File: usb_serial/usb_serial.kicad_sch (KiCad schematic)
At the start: 13 parts, among them J1 47589-1001, J3 Conn_01x04_Pin, U1 FT232RL

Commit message: BOM generated
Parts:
- C1: Manufacturer (none) -> Kemet; Package (none) -> 0402; Part (none) -> C0402C103K5RECAUTO
- C2: Manufacturer (none) -> Samsung Electro-Mechanics; Package (none) -> 0805; Part (none) -> CL21A475KAQNNNE
- C3, C4: Manufacturer (none) -> Samsung Electro-Mechanics; Package (none) -> 0402; Part (none) -> CL05B104KP5NNNC
- D1, D2, D3: Manufacturer (none) -> LS R976-NR-1-0-20-R18; Package (none) -> 0805; Part (none) -> ams-OSRAM USA INC.
- J1: Manufacturer (none) -> Molex; Package None -> -; Part (none) -> 47589-1001
- J3: Manufacturer (none) -> Würth Elektronik; Package (none) -> -; Part (none) -> 61300411121
- R1, R2: Manufacturer (none) -> YAGEO; Package (none) -> 0402; Part (none) -> RC0402JR-0710KL
- R3: value 2.2k -> 1k; Manufacturer (none) -> YAGEO; Package (none) -> 0402; Part (none) -> RC0402JR-0710KL
- U1: Manufacturer (none) -> FTDI; Package (none) -> SSOP-28; Part (none) -> FT232RL

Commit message: BOM Fix  - wrong reg value
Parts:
- R1, R2, R3: Manufacturer YAGEO -> UNI-ROYAL(Uniroyal Elec); Part RC0402JR-0710KL -> 0402WGF1001TCE
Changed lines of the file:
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@@
 			)
 		)
-		(property "Manufacturer" "YAGEO"
+		(property "Manufacturer" "UNI-ROYAL(Uniroyal Elec)"
 			(at 226.06 102.87 0)
 			(effects
@@
 			)
 		)
-		(property "Part" "RC0402JR-0710KL"
+		(property "Part" "0402WGF1001TCE"
 			(at 226.06 102.87 0)
 			(effects
@@
 			)
 		)
-		(property "Manufacturer" "YAGEO"
+		(property "Manufacturer" "UNI-ROYAL(Uniroyal Elec)"
 			(at 102.87 86.36 0)
 			(effects
@@
 			)
 		)
-		(property "Part" "RC0402JR-0710KL"
+		(property "Part" "0402WGF1001TCE"
 			(at 102.87 86.36 0)
 			(effects
@@
 			)
 		)
-		(property "Manufacturer" "YAGEO"
+		(property "Manufacturer" "UNI-ROYAL(Uniroyal Elec)"
 			(at 254 102.87 0)
 			(effects
@@
 			)
 		)
-		(property "Part" "RC0402JR-0710KL"
+		(property "Part" "0402WGF1001TCE"
 			(at 254 102.87 0)
 			(effects

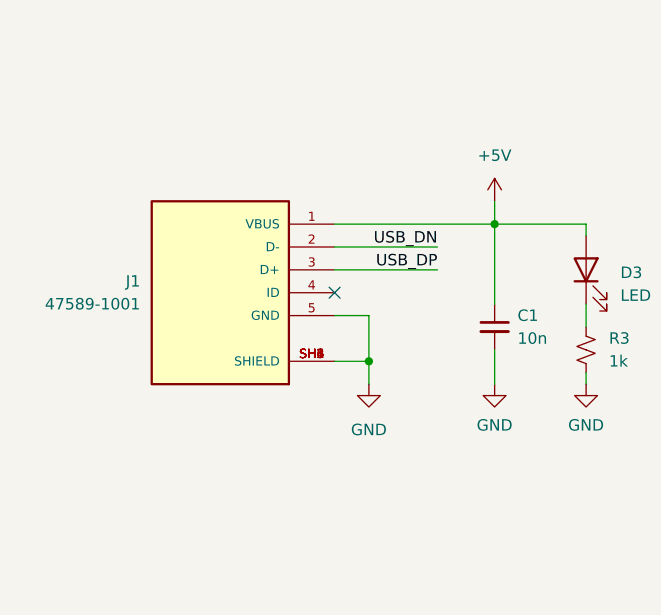
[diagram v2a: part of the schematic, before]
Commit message: JLCPCB adaptation - USB part changed
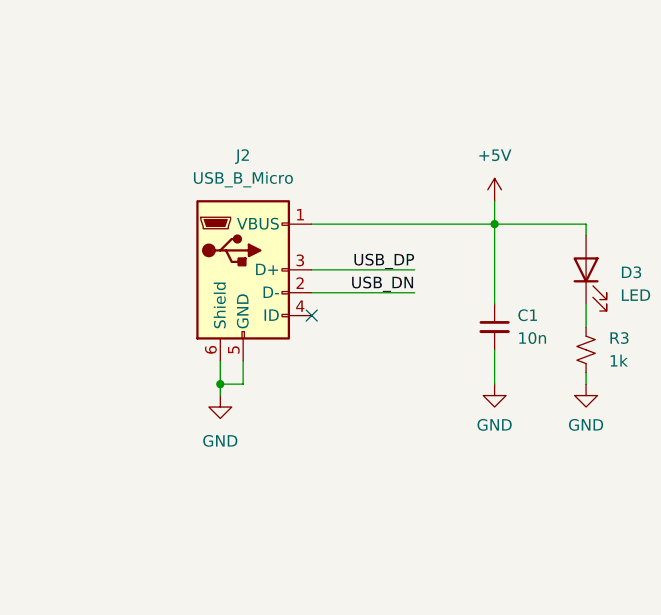
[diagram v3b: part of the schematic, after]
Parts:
- removed J1: 47589-1001, user_footprints:MOLEX_47589-1001, symbol 47589-1001:47589-1001
- added J2: USB_B_Micro, Connector_USB:USB_Micro-B_Amphenol_10118194-0001LF_Horizontal, symbol Connector:USB_B_Micro
- C1: footprint Capacitor_SMD:C_0402_1005Metric -> Capacitor_SMD:C_0603_1608Metric; Manufacturer Kemet -> FH (Guangdong Fenghua Advanced Tech); Package 0402 -> 0603; Part C0402C103K5RECAUTO -> 0603B103K500NT
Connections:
- net +5V: now also J2.1 (VBUS)
- net GND: now also J2.5 (GND), J2.6 (Shield)
- net USB_DN: now also J2.2 (D-)
- net USB_DP: now also J2.3 (D+)

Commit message: JLCPCB Ready - bom/Gerber/PnP/Schematic regenerated
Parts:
- C1: LCSC (none) -> C57112
- C2: LCSC (none) -> C1779
- C3, C4: LCSC (none) -> C133086
- D1, D2, D3: LCSC (none) -> C2899997
- J2: LCSC (none) -> C132563
- J3: LCSC (none) -> C5184785
- R1, R2, R3: LCSC (none) -> C11702
- U1: LCSC (none) -> C8690
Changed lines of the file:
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@@
 			)
 		)
+		(property "LCSC" "C133086"
+			(at 128.27 101.6 0)
+			(effects
+				(font
+					(size 1.27 1.27)
+				)
+				(hide yes)
+			)
+		)
 		(pin "1"
 		)
@@
 			)
 		)
+		(property "LCSC" "C8690"
+			(at 158.75 85.09 0)
+			(effects
+				(font
+					(size 1.27 1.27)
+				)
+				(hide yes)
+			)
+		)
 		(pin "8"
 		)
@@
 			)
 		)
+		(property "LCSC" "C2899997"
+			(at 102.87 77.47 0)
+			(effects
+				(font
+					(size 1.27 1.27)
+				)
+				(hide yes)
+			)
+		)
 		(pin "2"
 		)
@@
 			)
 		)
+		(property "LCSC" "C11702"
+			(at 226.06 102.87 0)
+			(effects
+				(font
+					(size 1.27 1.27)
+				)
+				(hide yes)
+			)
+		)
 		(pin "1"
 		)
@@
 			)
 		)
+		(property "LCSC" "C2899997"
+			(at 254 93.98 0)
+			(effects
+				(font
+					(size 1.27 1.27)
+				)
+				(hide yes)
+			)
+		)
 		(pin "2"
 		)
@@
 			)
 		)
+		(property "LCSC" "C1779"
+			(at 217.17 62.23 0)
+			(effects
+				(font
+					(size 1.27 1.27)
+				)
+				(hide yes)
+			)
+		)
 		(pin "1"
 		)
@@
 			)
 		)
+		(property "LCSC" "C132563"
+			(at 64.77 77.47 0)
+			(effects
+				(font
+					(size 1.27 1.27)
+				)
+				(hide yes)
+			)
+		)
 		(pin "1"
 		)
@@
 			)
 		)
+		(property "LCSC" "C133086"
+			(at 227.33 62.23 0)
+			(effects
+				(font
+					(size 1.27 1.27)
+				)
+				(hide yes)
+			)
+		)
 		(pin "1"
 		)
@@
 			)
 		)
+		(property "LCSC" "C11702"
+			(at 102.87 86.36 0)
+			(effects
+				(font
+					(size 1.27 1.27)
+				)
+				(hide yes)
+			)
+		)
 		(pin "1"
 		)
@@
 			)
 		)
+		(property "LCSC" "C5184785"
+			(at 228.6 134.62 0)
+			(effects
+				(font
+					(size 1.27 1.27)
+				)
+				(hide yes)
+			)
+		)
 		(pin "2"
 		)
@@
 			)
 		)
+		(property "LCSC" "C11702"
+			(at 254 102.87 0)
+			(effects
+				(font
+					(size 1.27 1.27)
+				)
+				(hide yes)
+			)
+		)
 		(pin "1"
 		)
@@
 			)
 		)
+		(property "LCSC" "C57112"
+			(at 92.71 83.82 0)
+			(effects
+				(font
+					(size 1.27 1.27)
+				)
+				(hide yes)
+			)
+		)
 		(pin "1"
 		)
@@
 			(at 226.06 93.98 0)
 			(effects
+				(font
+					(size 1.27 1.27)
+				)
+				(hide yes)
+			)
+		)
+		(property "LCSC" "C2899997"
+			(at 226.06 93.98 0)
+			(effects

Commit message: [FIX] Changed 4pin 2.54mm header from vertical one to a right-angled one
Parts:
- J3: LCSC C5184785 -> C91552; Manufacturer Würth Elektronik -> BOOMELE(Boom Precision Elec); Part 61300411121 -> 2.54-1*4P反弯排针
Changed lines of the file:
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@@
 			)
 		)
-		(property "Manufacturer" "Würth Elektronik"
+		(property "Manufacturer" "BOOMELE(Boom Precision Elec)"
 			(at 228.6 134.62 0)
 			(effects
@@
 			)
 		)
-		(property "Part" "61300411121"
+		(property "Part" "2.54-1*4P反弯排针"
 			(at 228.6 134.62 0)
 			(effects
@@
 			)
 		)
-		(property "LCSC" "C5184785"
+		(property "LCSC" "C91552"
 			(at 228.6 134.62 0)
 			(effects

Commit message: Updated Legend
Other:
- title: (none) -> USB to Serial Converter Board
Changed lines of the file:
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@@
 	(generator_version "8.0")
 	(paper "A4")
+	(title_block
+		(title "USB to Serial Converter Board")
+	)
 	(junction
 		(at 156.21 110.49)
